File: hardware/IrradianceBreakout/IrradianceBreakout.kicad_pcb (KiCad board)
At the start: 0 parts

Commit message: check breakout board layout
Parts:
- added C1: 10u, Capacitor_SMD:C_0805_2012Metric_Pad1.18x1.45mm_HandSolder, F.Cu at (131.1, 33.9)
- added C2: 100n, Capacitor_SMD:C_0603_1608Metric_Pad1.08x0.95mm_HandSolder, F.Cu at (131.1, 31.6)
- added D1: Red, LED_SMD:LED_0603_1608Metric, F.Cu at (132.6, 38.7)
- added D2: D5V0P4UR6SO-7, LHRS_ICs:D5V0P4UR6SO-7, F.Cu at (126.8, 37.5)
- added J1: Nano-Fit 1x5, Connector_Molex:Molex_Nano-Fit_105313-xx05_1x05_P2.50mm_Horizontal, F.Cu at (121.6, 41.2)
- added Q1: DMP3099L, Package_TO_SOT_SMD:SOT-23, F.Cu at (126.8, 41.6)
- added R2: 2.2k, Resistor_SMD:R_0603_1608Metric_Pad0.98x0.95mm_HandSolder, F.Cu at (128.0, 30.0)
- added R3: 2.2k, Resistor_SMD:R_0603_1608Metric_Pad0.98x0.95mm_HandSolder, F.Cu at (125.2, 29.2)
- added R4: 10k, Resistor_SMD:R_0603_1608Metric_Pad0.98x0.95mm_HandSolder, F.Cu at (130.6, 41.8)
- added R5: 1k, Resistor_SMD:R_0603_1608Metric_Pad0.98x0.95mm_HandSolder, F.Cu at (132.0, 36.1)
- added U1: TSL25911FN, OptoDevice:AMS_TSL25911FN, F.Cu at (126.6, 33.1)
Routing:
- net +3.3V: track 0.00 -> 35.0 mm, vias 0 -> 2
- net /SDA: track 0.00 -> 26.1 mm, vias 0 -> 2
- net /ALS_INT: track 0.00 -> 23.7 mm, vias 0 -> 2
- net /SCL: track 0.00 -> 15.9 mm, vias 0 -> 2
- net GND: track 0.00 -> 10.5 mm, vias 0 -> 2
- net Net-(Q1-D): track 0.00 -> 8.30 mm, vias 0 -> 2
- net Net-(D1-A): track 0.00 -> 1.94 mm
- added copper zone on F.Cu, net GND
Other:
- board outline added: 26.2 x 19.4 mm
- copper layers 0 -> 2

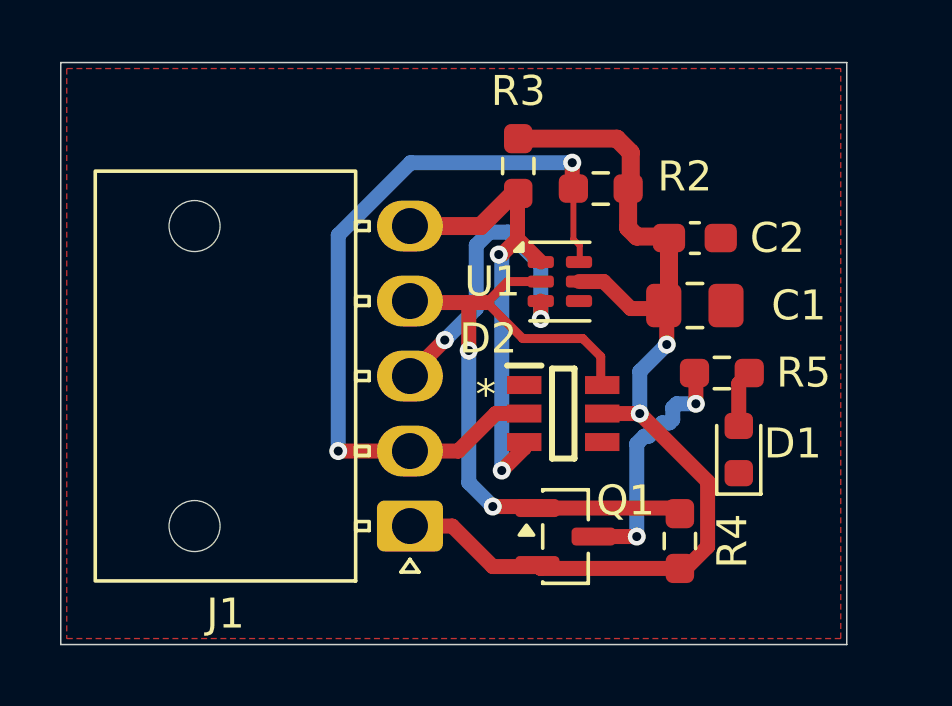
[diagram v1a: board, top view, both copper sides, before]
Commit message: Main board placement + silkscreen, breakout ground plane, DRC rule updates
- Grouped placement and condensed outline (2 mm rounded corners)
- Silkscreen refs moved next to their parts, pin labels added
- Interrupt removed from main board and breakout (test point instead)
- Breakout: B.Cu ground plane + stitching vias
- Default clearance / hole clearance lowered to 0.15 mm
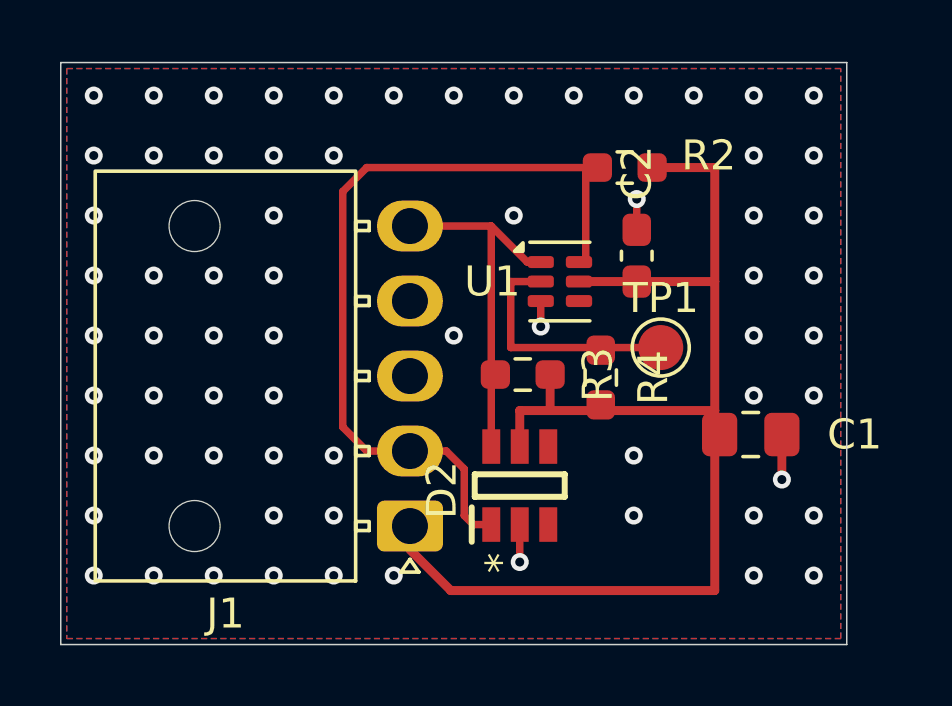
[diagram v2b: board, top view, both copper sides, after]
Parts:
- removed D1: Red, LED_SMD:LED_0603_1608Metric
- removed Q1: DMP3099L, Package_TO_SOT_SMD:SOT-23
- removed R5: 1k, Resistor_SMD:R_0603_1608Metric_Pad0.98x0.95mm_HandSolder
- added TP1: INT, TestPoint:TestPoint_Pad_D1.5mm, F.Cu at (130.0, 35.3)
- moved R3 6.95 mm to (125.4, 36.2), turned to 180 degrees
- moved R4 6.05 mm to (128.0, 36.3)
- moved C1 4.69 mm to (133.0, 38.2)
- moved D2 2.80 mm to (125.3, 39.9), turned to 90 degrees
- moved C2 2.02 mm to (129.2, 32.2), turned to 90 degrees
- moved R2 1.06 mm to (128.8, 29.3)
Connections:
- D2 pad 1: GND -> /SDA
- D2 pad 2: /SDA -> GND
- D2 pad 3: /SCL -> unconnected-(D2-Pad3)
- D2 pad 6: /ALS_INT -> /SCL
- J1 pad 4: /ALS_INT -> unconnected-(J1-Pin_4-Pad4)
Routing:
- net /ALS_INT: track 23.7 -> 8.29 mm, vias 2 -> 0
- net Net-(Q1-D): track 8.30 -> 0.00 mm, vias 2 -> 0
- net GND: track 10.5 -> 4.62 mm, vias 2 -> 68
- net +3.3V: track 35.0 -> 40.2 mm, vias 2 -> 0
- net /SCL: track 15.9 -> 12.0 mm, vias 2 -> 0
- net Net-(D1-A): track 1.94 -> 0.00 mm
- net /SDA: track 26.1 -> 26.6 mm, vias 2 -> 0
- added copper zone on B.Cu, net GND
